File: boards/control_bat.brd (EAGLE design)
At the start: 101.6 x 30.5 mm, 17 parts, among them U1 579-MCP1703T-3002ECB, U2 771-LPC824M201JDH20J, U3 888-XB24CZ7PIS-004

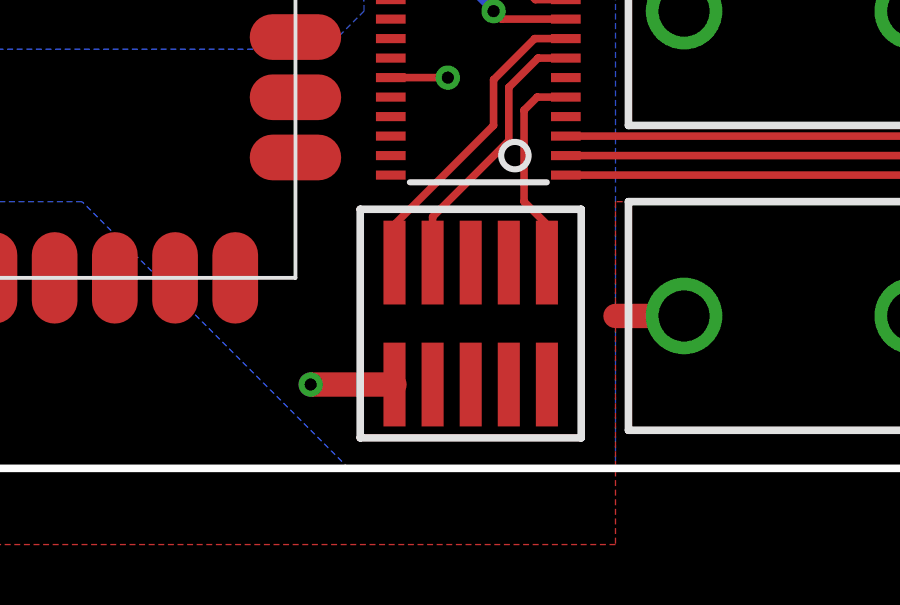
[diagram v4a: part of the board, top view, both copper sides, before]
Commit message: Probably not a bad idea to have a pullup on the reset line.
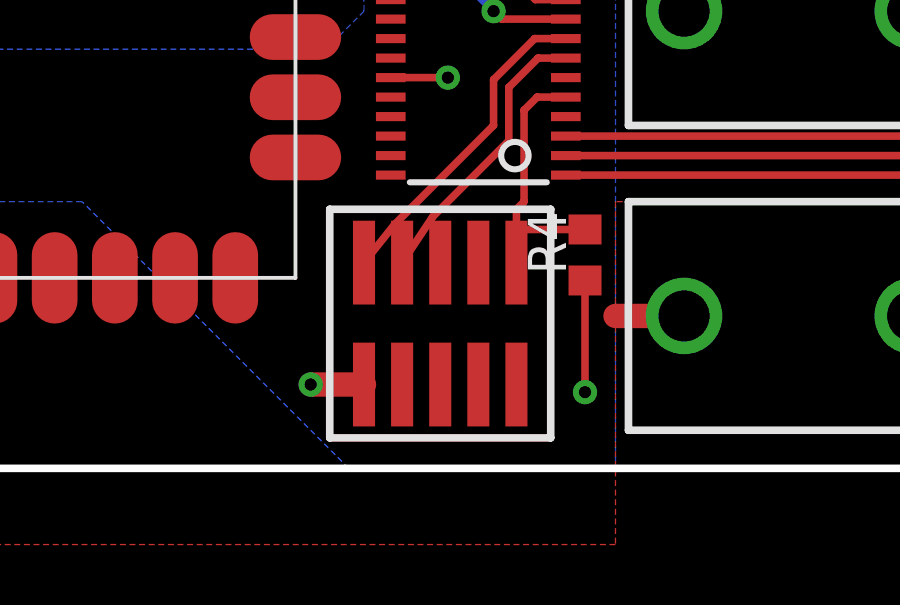
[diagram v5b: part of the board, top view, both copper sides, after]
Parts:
- added R4: 71-CRCW0603-10K-E3, rcl:R0603
- moved JP3 1.02 mm to (38.6, 4.83)
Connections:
- net +3V3: now also R4.1
- net RST: now also R4.2
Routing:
- net +3V3: track 26.7 -> 29.4 mm, vias 4 -> 5
- net RST: track 6.97 -> 9.05 mm
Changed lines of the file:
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@@
 <attribute name="VALUE" x="95.56" y="18.99" size="1.27" layer="27" rot="R270"/>
 </element>
-<element name="JP3" library="torpedo" package="FTSH-105-01-XXX-DV-K" value="FTSH-105-01-L" x="39.624" y="4.826" smashed="yes"/>
+<element name="JP3" library="torpedo" package="FTSH-105-01-XXX-DV-K" value="FTSH-105-01-L" x="38.608" y="4.826" smashed="yes"/>
 <element name="BAT3" library="SparkFun-Electromechanical" package="BATTERY-AAA-KIT" value="" x="68.326" y="5.08" smashed="yes" rot="R180">
 <attribute name="PROD_ID" value="BATT-08571" x="68.326" y="5.08" size="1.778" layer="27" rot="R180" display="off"/>
@@
 <attribute name="NAME" x="41.91" y="16.51" size="1.27" layer="25" ratio="18"/>
 </element>
+<element name="R4" library="rcl" package="R0603" value="71-CRCW0603-10K-E3" x="43.434" y="7.112" rot="R90"/>
 </elements>
 <signals>
@@
 <wire x1="93.98" y1="24.042" x2="93.98" y2="20.32" width="0.8128" layer="1"/>
 <via x="93.98" y="20.32" extent="1-16" drill="0.8128"/>
-<wire x1="37.084" y1="2.794" x2="34.29" y2="2.794" width="0.8128" layer="1"/>
+<wire x1="36.068" y1="2.794" x2="34.29" y2="2.794" width="0.8128" layer="1"/>
 <via x="34.29" y="2.794" extent="1-16" drill="0.4064"/>
 <contactref element="JP1" pad="1"/>
@@
 <wire x1="10.414" y1="10.668" x2="17.272" y2="10.668" width="0.254" layer="1"/>
 <wire x1="17.272" y1="10.668" x2="17.78" y2="10.16" width="0.254" layer="1"/>
+<contactref element="R4" pad="1"/>
+<wire x1="43.434" y1="6.262" x2="43.434" y2="2.54" width="0.254" layer="1"/>
+<via x="43.434" y="2.54" extent="1-16" drill="0.4064"/>
 </signal>
 <signal name="VIN">
@@
 <signal name="SWDIO">
 <contactref element="JP3" pad="2"/>
-<wire x1="37.084" y1="6.858" x2="37.084" y2="8.128" width="0.254" layer="1"/>
+<wire x1="36.068" y1="6.858" x2="37.084" y2="8.128" width="0.254" layer="1"/>
 <wire x1="37.084" y1="8.128" x2="40.386" y2="11.43" width="0.254" layer="1"/>
 <wire x1="40.386" y1="11.43" x2="40.386" y2="12.954" width="0.254" layer="1"/>
@@
 <signal name="SWCLK">
 <contactref element="JP3" pad="4"/>
-<wire x1="38.354" y1="6.858" x2="38.354" y2="8.382" width="0.254" layer="1"/>
+<wire x1="37.338" y1="6.858" x2="38.354" y2="8.382" width="0.254" layer="1"/>
 <wire x1="38.354" y1="8.382" x2="40.894" y2="10.922" width="0.254" layer="1"/>
 <wire x1="40.894" y1="10.922" x2="40.894" y2="12.7" width="0.254" layer="1"/>
@@
 <signal name="RST">
 <contactref element="JP3" pad="10"/>
-<wire x1="42.164" y1="6.858" x2="42.164" y2="8.128" width="0.254" layer="1"/>
-<wire x1="42.164" y1="8.128" x2="41.402" y2="8.89" width="0.254" layer="1"/>
+<wire x1="41.148" y1="6.858" x2="41.148" y2="7.874" width="0.254" layer="1"/>
+<wire x1="41.148" y1="7.962" x2="41.148" y2="8.636" width="0.254" layer="1"/>
+<wire x1="41.148" y1="8.636" x2="41.402" y2="8.89" width="0.254" layer="1"/>
 <wire x1="41.402" y1="8.89" x2="41.402" y2="11.938" width="0.254" layer="1"/>
 <wire x1="41.402" y1="11.938" x2="41.839" y2="12.375" width="0.254" layer="1"/>
 <contactref element="U2" pad="5"/>
 <wire x1="41.839" y1="12.375" x2="42.7958" y2="12.375" width="0.254" layer="1"/>
+<contactref element="R4" pad="2"/>
+<wire x1="43.434" y1="7.962" x2="41.148" y2="7.962" width="0.254" layer="1"/>
+<wire x1="41.148" y1="7.962" x2="41.148" y2="7.874" width="0.254" layer="1"/>
 </signal>
 <signal name="RX">

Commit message: Fix overlap
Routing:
- net SWDIO: track 10.8 -> 13.1 mm
- net SWCLK: track 9.51 -> 11.3 mm
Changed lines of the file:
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@@
 <signal name="SWDIO">
 <contactref element="JP3" pad="2"/>
-<wire x1="36.068" y1="6.858" x2="37.084" y2="8.128" width="0.254" layer="1"/>
-<wire x1="37.084" y1="8.128" x2="40.386" y2="11.43" width="0.254" layer="1"/>
-<wire x1="40.386" y1="11.43" x2="40.386" y2="12.954" width="0.254" layer="1"/>
 <wire x1="40.386" y1="12.954" x2="41.757" y2="14.325" width="0.254" layer="1"/>
 <contactref element="U2" pad="8"/>
 <wire x1="41.757" y1="14.325" x2="42.7958" y2="14.325" width="0.254" layer="1"/>
+<wire x1="36.068" y1="6.858" x2="36.068" y2="8.89" width="0.254" layer="1"/>
+<wire x1="36.068" y1="8.89" x2="36.322" y2="9.144" width="0.254" layer="1"/>
+<wire x1="36.322" y1="9.144" x2="40.132" y2="9.144" width="0.254" layer="1"/>
+<wire x1="40.132" y1="9.144" x2="40.386" y2="9.398" width="0.254" layer="1"/>
+<wire x1="40.386" y1="9.398" x2="40.386" y2="12.954" width="0.254" layer="1"/>
 </signal>
 <signal name="SWCLK">
 <contactref element="JP3" pad="4"/>
-<wire x1="37.338" y1="6.858" x2="38.354" y2="8.382" width="0.254" layer="1"/>
-<wire x1="38.354" y1="8.382" x2="40.894" y2="10.922" width="0.254" layer="1"/>
-<wire x1="40.894" y1="10.922" x2="40.894" y2="12.7" width="0.254" layer="1"/>
 <wire x1="40.894" y1="12.7" x2="41.869" y2="13.675" width="0.254" layer="1"/>
 <contactref element="U2" pad="7"/>
 <wire x1="41.869" y1="13.675" x2="42.7958" y2="13.675" width="0.254" layer="1"/>
+<wire x1="37.338" y1="6.858" x2="37.338" y2="8.382" width="0.254" layer="1"/>
+<wire x1="37.338" y1="8.382" x2="37.592" y2="8.636" width="0.254" layer="1"/>
+<wire x1="37.592" y1="8.636" x2="40.386" y2="8.636" width="0.254" layer="1"/>
+<wire x1="40.386" y1="8.636" x2="40.894" y2="9.144" width="0.254" layer="1"/>
+<wire x1="40.894" y1="9.144" x2="40.894" y2="12.7" width="0.254" layer="1"/>
 </signal>
 <signal name="RST">
@@
 </signal>
 </signals>
+<errors>
+</errors>
 </board>
 </drawing>
